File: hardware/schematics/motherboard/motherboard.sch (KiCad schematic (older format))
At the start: 11 parts

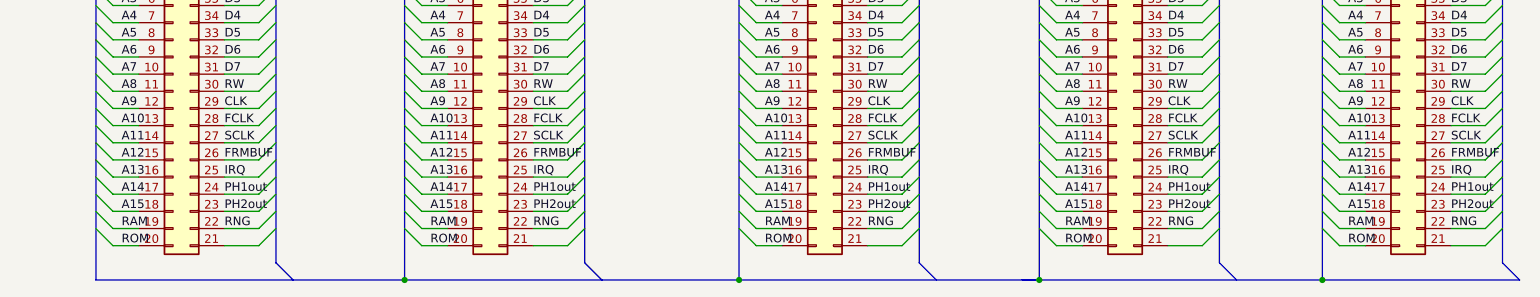
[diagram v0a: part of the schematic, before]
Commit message: I added the initial versions on the cpu and memory card
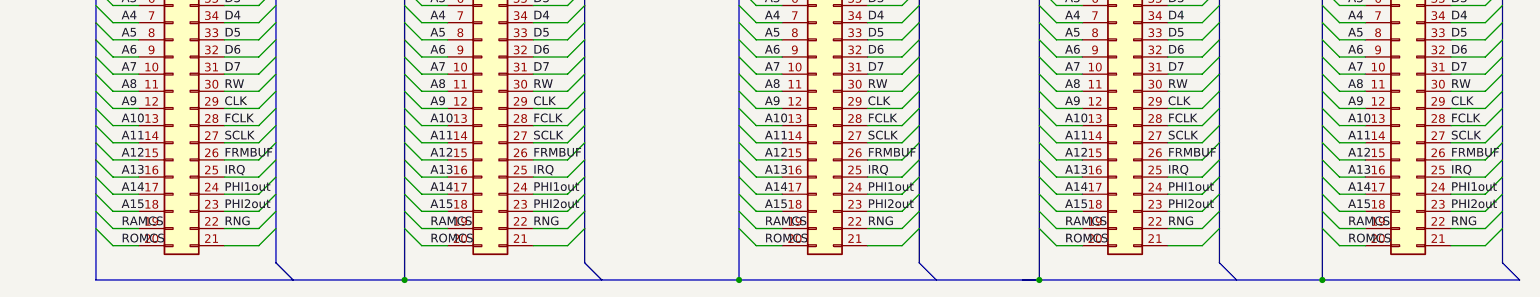
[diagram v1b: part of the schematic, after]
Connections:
- net PH1out renamed PHI1out
- net PH2out renamed PHI2out
- net RAM renamed RAMCS
- net ROM renamed ROMCS
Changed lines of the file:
@@
 FRMBUF
 Text Label 2500 4650 0    50   ~ 0
-RAM
+RAMCS
 Text Label 2500 4750 0    50   ~ 0
-ROM
+ROMCS
 Entry Wire Line
 	2250 2450 2350 2350
@@
 FRMBUF
 Text Label 4300 4650 0    50   ~ 0
-RAM
+RAMCS
 Text Label 4300 4750 0    50   ~ 0
-ROM
+ROMCS
 Entry Wire Line
 	4050 2550 4150 2450
@@
 FRMBUF
 Text Label 6250 4650 0    50   ~ 0
-RAM
+RAMCS
 Text Label 6250 4750 0    50   ~ 0
-ROM
+ROMCS
 Entry Wire Line
 	6000 2450 6100 2350
@@
 FRMBUF
 Text Label 8000 4650 0    50   ~ 0
-RAM
+RAMCS
 Text Label 8000 4750 0    50   ~ 0
-ROM
+ROMCS
 Entry Wire Line
 	7750 2450 7850 2350
@@
 IRQ
 Text Label 6850 4450 0    50   ~ 0
-PH1out
+PHI1out
 Text Label 4900 4450 0    50   ~ 0
-PH1out
+PHI1out
 Text Label 3100 4450 0    50   ~ 0
-PH1out
+PHI1out
 Text Label 8600 4450 0    50   ~ 0
-PH1out
+PHI1out
 Text Label 3100 4550 0    50   ~ 0
-PH2out
+PHI2out
 Text Label 4900 4550 0    50   ~ 0
-PH2out
+PHI2out
 Text Label 6850 4550 0    50   ~ 0
-PH2out
+PHI2out
 Text Label 8600 4550 0    50   ~ 0
-PH2out
+PHI2out
 $Comp
 L Connector_Generic:Conn_02x20_Counter_Clockwise J?
@@
 FRMBUF
 Text Label 9650 4650 0    50   ~ 0
-RAM
+RAMCS
 Text Label 9650 4750 0    50   ~ 0
-ROM
+ROMCS
 Entry Wire Line
 	9400 2450 9500 2350
@@
 IRQ
 Text Label 10250 4450 0    50   ~ 0
-PH1out
+PHI1out
 Text Label 10250 4550 0    50   ~ 0
-PH2out
+PHI2out
 Wire Bus Line
 	7850 4950 9500 4950

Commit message: I started working on the PCBs
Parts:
- added J3: Conn_01x02_Male, Connector_PinHeader_2.54mm:PinHeader_1x02_P2.54mm_Vertical, symbol Connector:Conn_01x02_Male
- C1, C2, C3, C4: renamed from C?; value C -> 0.1uF; footprint (none) -> Capacitor_THT:C_Disc_D3.8mm_W2.6mm_P2.50mm
- C5: renamed from C?; value C -> 0.1uF; footprint (none) -> Capacitor_THT:C_Disc_D3.0mm_W1.6mm_P2.50mm
- J1: renamed from J?; footprint (none) -> Connector_BarrelJack:BarrelJack_CUI_PJ-102AH_Horizontal
- J2: renamed from J?; footprint (none) -> motherboard:PinSocket_2x20_P2.54mm_Vertical_Counter_Clockwise
- J4, J5, J6, J7: renamed from J?; footprint (none) -> Connector_PinSocket_2.54mm:PinSocket_2x20_P2.54mm_Vertical
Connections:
- net Earth: now also J3.2 (Pin_2)
- net +5V renamed VCC
- net VCC: now also J3.1 (Pin_1)
- no-connect marks 0 -> 5
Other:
- moved on the sheet: C1, C2, C3, C4, C5, J1, J2, J4, J5, J6, J7
